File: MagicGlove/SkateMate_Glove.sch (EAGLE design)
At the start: 42 parts, among them IC1 BU33TD3WG, IC2 LMV321M5, U2 ATMEGA328PB-AU

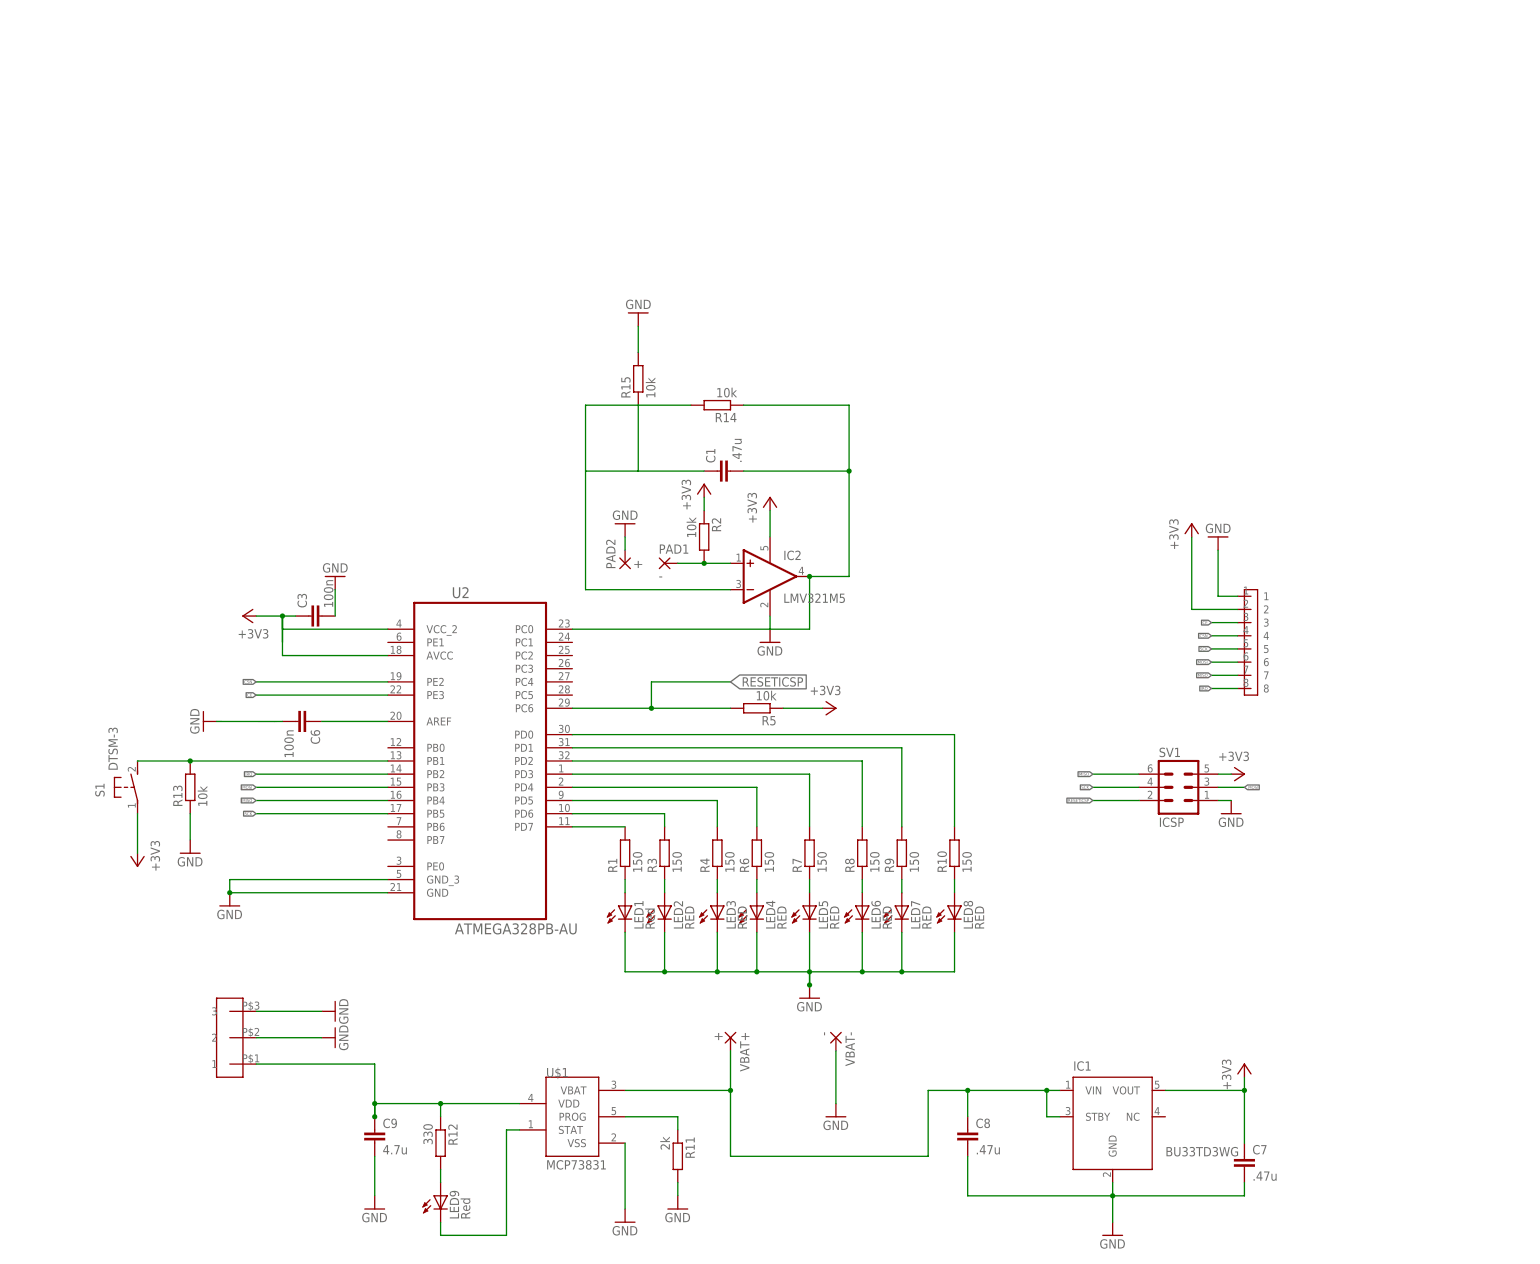
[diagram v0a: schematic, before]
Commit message: New Version of MagicGlove Print 	- Rewired the analog part 	- Smaller Layout alltogether Initial Version of MagicGlove Receiver Print 	- Some GPIO Pads for anything that might be added
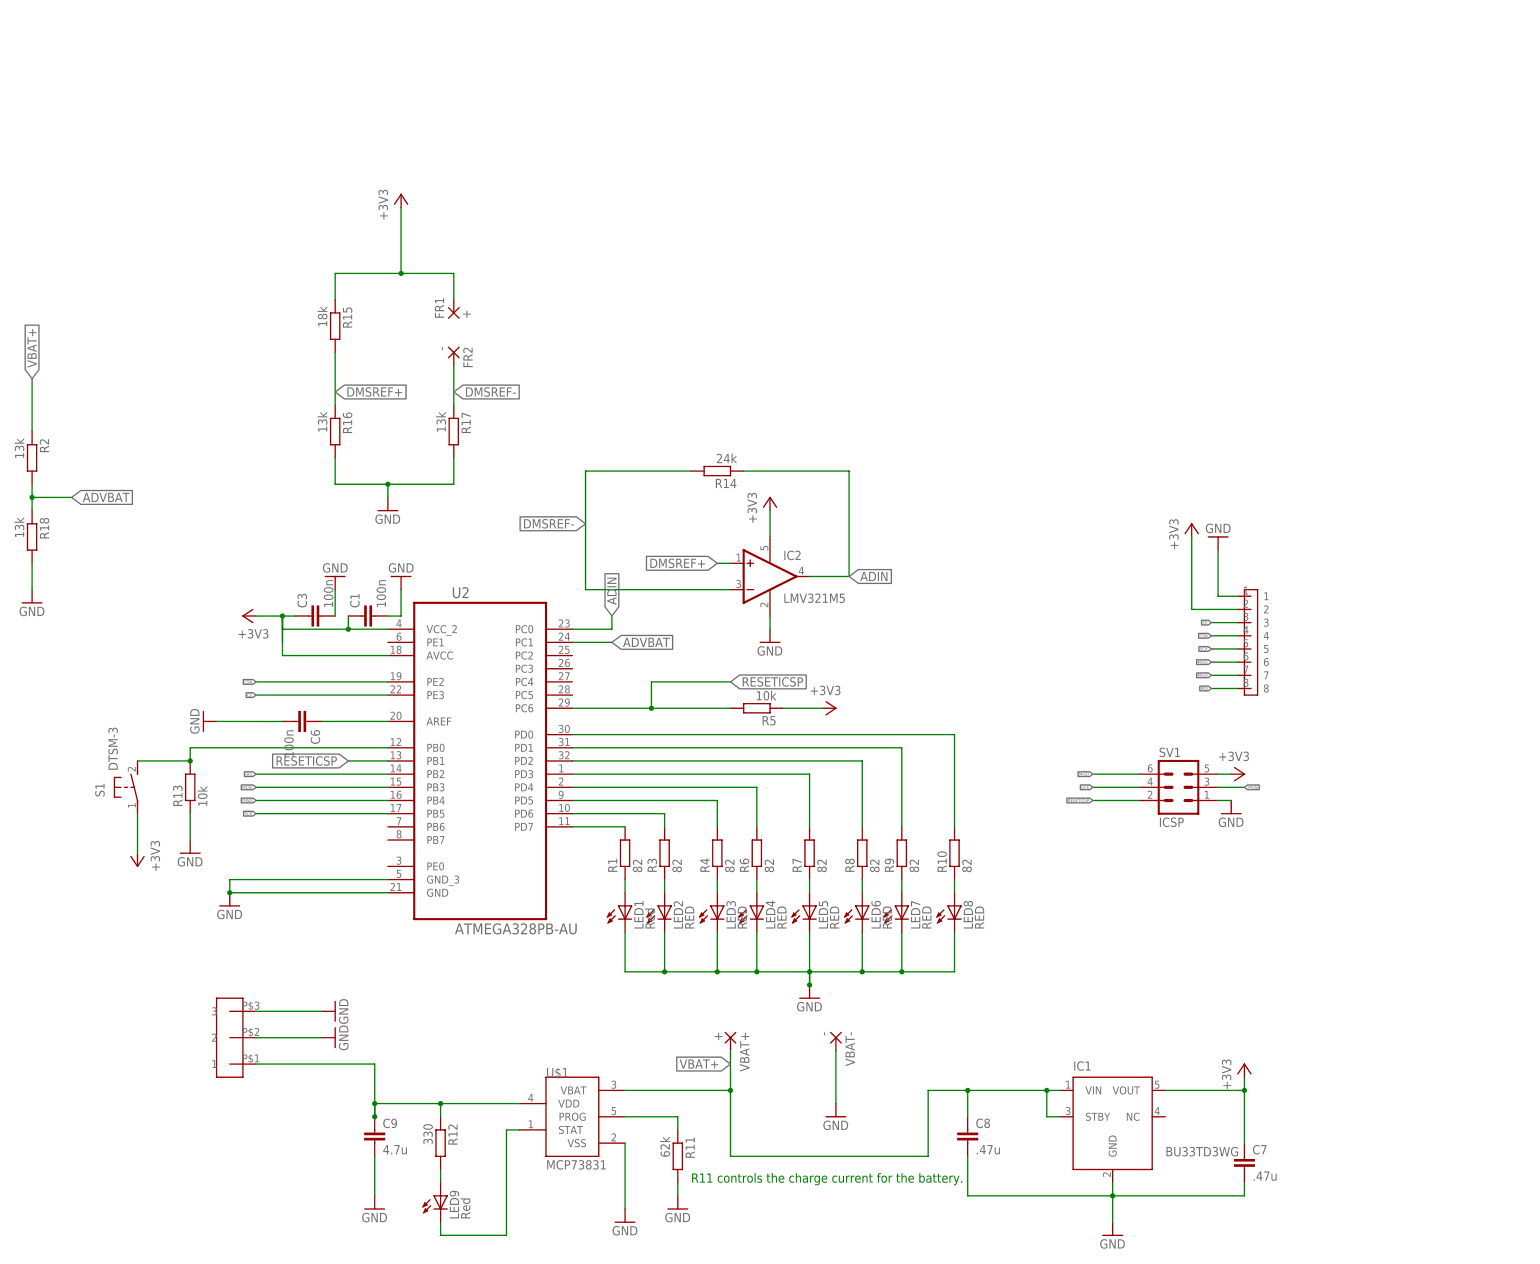
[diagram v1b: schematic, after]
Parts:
- removed PAD1: -, wirepad:1,6/0,8
- removed PAD2: +, wirepad:1,6/0,8
- added FR1: +, wirepad:1,6/0,8
- added FR2: -, wirepad:1,6/0,8
- added R16, R17, R18: 13k, eagle-ltspice:RR0603
- C1: value .47u -> 100n
- R1, R10, R3, R4, R6, R7, R8, R9: value 150 -> 82
- R11: value 2k -> 62k
- R14: value 10k -> 24k
- R15: value 10k -> 18k
- R2: value 10k -> 13k
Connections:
- removed net N$14: C1.2, IC2.OUT, R14.1, U2.PC0
- removed net N$21: C8.1, IC1.STBY, IC1.VIN, U$1.VBAT, VBAT+.P
- removed net N$26: IC2.+IN, PAD1.P, R2.2
- removed net N$5: C1.1, IC2.-IN, R14.2, R15.1
- new net ADIN: IC2.OUT, R14.1, U2.PC0
- new net ADVBAT: R18.1, R2.2, U2.PC1
- new net DMSREF+: IC2.+IN, R15.2, R16.1
- new net DMSREF-: FR2.P, IC2.-IN, R14.2, R17.1
- new net VBAT+: C8.1, IC1.STBY, IC1.VIN, R2.1, U$1.VBAT, VBAT+.P
- net +3V3: now also C1.1, FR1.P, R15.1; no longer R2.1
- net GND: now also C1.2, R16.2, R17.2, R18.2; no longer PAD2.P, R15.2
- net N$3: now also U2.PB0; no longer U2.PB1
- net RESETICSP: now also U2.PB1
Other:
- note added: "R11 controls the charge current for the battery."
- moved on the sheet: C1, R14, R15, R2

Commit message: style
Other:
- moved on the sheet: C1, C3, C6, C7, C8, C9, FR1, FR2, IC1, IC2, LED1, LED2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
